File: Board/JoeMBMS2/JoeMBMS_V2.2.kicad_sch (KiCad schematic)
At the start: 40 parts, among them J1 5007620481, Q1 BSO615NG, Q2 BSO615NG, Q3 P-Chanel Mosfet, U1 Teensy3.2, U2 SN65HVD251, U3 DCDC 5V, U4 IS281-4

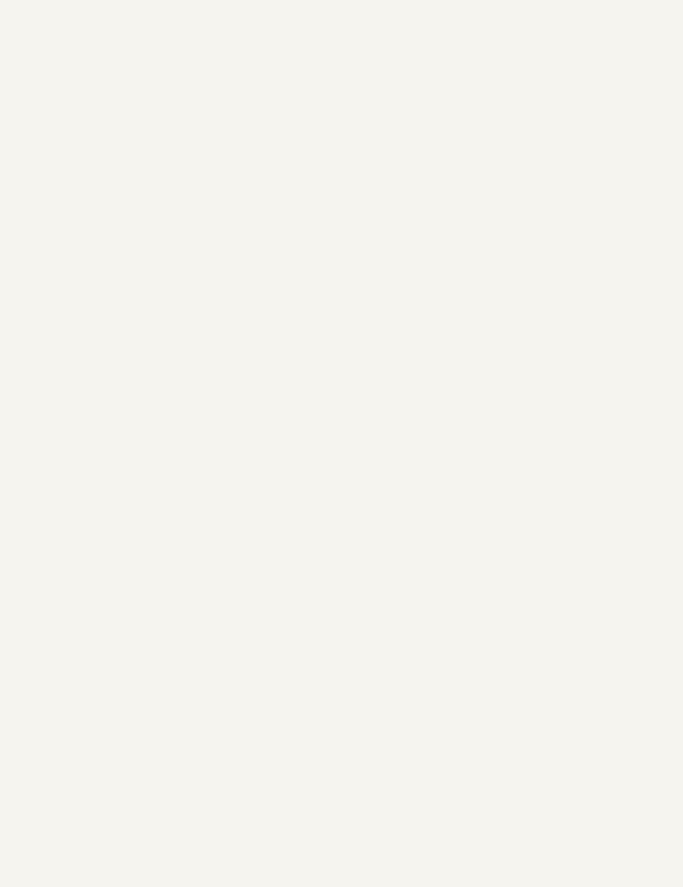
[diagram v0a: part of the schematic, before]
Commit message: Upgrade Teensy 3.2 -> 4.0
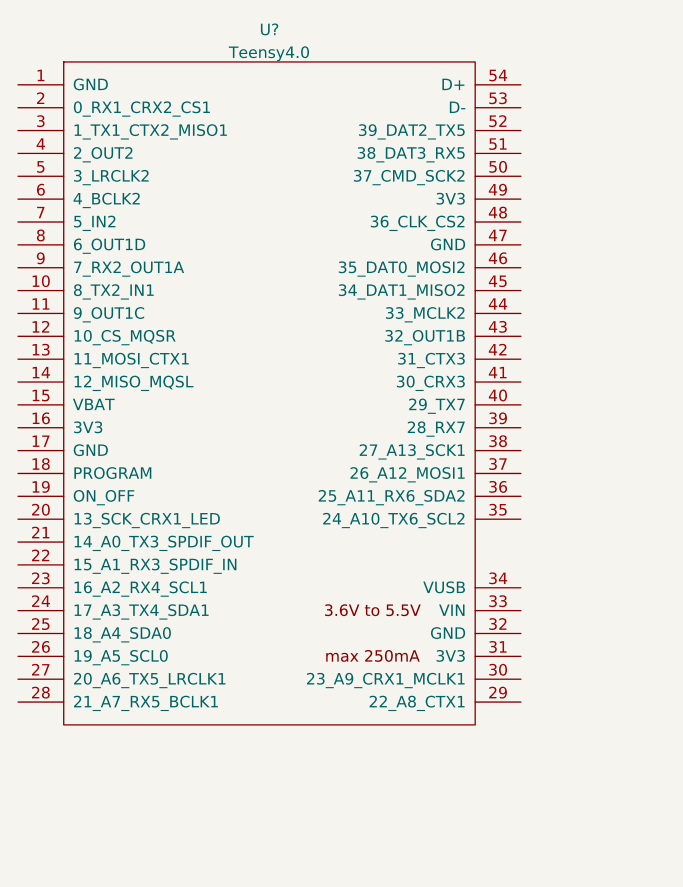
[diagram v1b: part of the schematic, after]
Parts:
- added U?: Teensy4.0, symbol Teensy:Teensy4.0
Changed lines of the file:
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@@
     (pin "1")
+  )
+  (symbol (lib_id "Teensy:Teensy4.0") (at -31.75 50.8 0) (unit 1)
+    (in_bom yes) (on_board yes) (fields_autoplaced)
+    (property "Reference" "U?" (id 0) (at -31.75 10.3972 0))
+    (property "Value" "Teensy4.0" (id 1) (at -31.75 12.9341 0))
+    (property "Footprint" "" (id 2) (at -41.91 45.72 0)
+      (effects (font (size 1.27 1.27)) hide)
+    )
+    (property "Datasheet" "" (id 3) (at -41.91 45.72 0)
+      (effects (font (size 1.27 1.27)) hide)
+    )
+    (pin "10")
+    (pin "11")
+    (pin "12")
+    (pin "13")
+    (pin "14")
+    (pin "15")
+    (pin "16")
+    (pin "17")
+    (pin "18")
+    (pin "19")
+    (pin "20")
+    (pin "21")
+    (pin "22")
+    (pin "23")
+    (pin "24")
+    (pin "25")
+    (pin "26")
+    (pin "27")
+    (pin "28")
+    (pin "29")
+    (pin "30")
+    (pin "31")
+    (pin "32")
+    (pin "33")
+    (pin "34")
+    (pin "35")
+    (pin "36")
+    (pin "37")
+    (pin "38")
+    (pin "39")
+    (pin "40")
+    (pin "41")
+    (pin "42")
+    (pin "43")
+    (pin "44")
+    (pin "45")
+    (pin "46")
+    (pin "47")
+    (pin "48")
+    (pin "49")
+    (pin "5")
+    (pin "50")
+    (pin "51")
+    (pin "52")
+    (pin "53")
+    (pin "54")
+    (pin "6")
+    (pin "7")
+    (pin "8")
+    (pin "9")
+    (pin "1")
+    (pin "2")
+    (pin "3")
+    (pin "4")
   )
   (symbol (lib_id "power:+5V") (at 116.84 151.13 0) (unit 1)
@@
       (reference "U4") (unit 1) (value "IS281-4 ") (footprint "TLP2934:TLP293-4")
     )
-  )
+    (path "/1e522045-1f8c-4d41-9233-66f025f5385c"
+      (reference "U?") (unit 1) (value "Teensy4.0") (footprint "")
+    )
+  )
